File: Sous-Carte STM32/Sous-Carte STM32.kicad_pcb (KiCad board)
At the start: 2 copper layers, 113 x 120.1 mm, 34 parts, among them J1 RJ45, P1 CONN_25X2, P2 CONN_25X2, P3 CONN_4, P5 CONN_25X2, P6 CONN_2, P7 CONN_2, P8 CONN_2

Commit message: routage sous carte stm 32
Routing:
- net B7: track 0.00 -> 203.1 mm, vias 0 -> 2
- net B9: track 0.00 -> 173.4 mm, vias 0 -> 4
- net E5: track 0.00 -> 163.1 mm, vias 0 -> 2
- net C12: track 17.5 -> 175.9 mm, vias 0 -> 4
- net B5: track 0.00 -> 152.1 mm, vias 0 -> 2
- net B3: track 0.00 -> 144.2 mm, vias 0 -> 2
- net UART2_TX: track 39.9 -> 180.0 mm, vias 0 -> 2
- net C8: track 0.00 -> 107.3 mm, vias 0 -> 2
- net UART3_TX: track 37.6 -> 139.5 mm, vias 0 -> 2
- net UART4_TX: track 106.8 -> 114.2 mm
- net UART4_RX: track 129.0 -> 133.9 mm
- net D2: track 227.7 -> 230.7 mm
- net E8: track 0.00 -> 1.96 mm
- net E14: track 0.00 -> 1.96 mm
- net E12: track 0.00 -> 1.96 mm
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
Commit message: plus que 3 piste a router 2 ou trois truc a revoir
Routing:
- net E10: track 0.00 -> 167.1 mm, vias 0 -> 2
- net E8: track 1.96 -> 167.5 mm, vias 0 -> 2
- net E6: track 0.00 -> 157.5 mm, vias 0 -> 2
- net E4: track 0.00 -> 150.5 mm, vias 0 -> 2
- net E9: track 0.00 -> 124.6 mm, vias 0 -> 4
- net E12: track 1.96 -> 123.9 mm, vias 0 -> 2
- net C4: track 0.00 -> 118.9 mm, vias 0 -> 4
- net E14: track 1.96 -> 114.0 mm
- net A0: track 0.00 -> 108.5 mm, vias 0 -> 4
- net E7: track 0.00 -> 107.6 mm, vias 0 -> 2
- net E11: track 0.00 -> 107.0 mm, vias 0 -> 2
- net A2: track 0.00 -> 97.7 mm, vias 0 -> 4
- net B10: track 1.96 -> 98.6 mm, vias 0 -> 2
- net E13: track 0.00 -> 95.8 mm, vias 0 -> 4
- net E15: track 0.00 -> 89.3 mm, vias 0 -> 4
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
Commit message: routage sous carte stm32 fini reste a agrandir la carte
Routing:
- net B4: track 0.00 -> 182.9 mm, vias 0 -> 2
- net B6: track 0.00 -> 175.3 mm, vias 0 -> 2
- net B8: track 0.00 -> 168.2 mm, vias 0 -> 2
- net A0: track 108.5 -> 103.2 mm
- net B9: track 173.1 -> 178.3 mm
- net UART2_RX: track 183.3 -> 187.0 mm
- net E5: track 163.4 -> 162.7 mm
- net E6: track 157.5 -> 158.1 mm

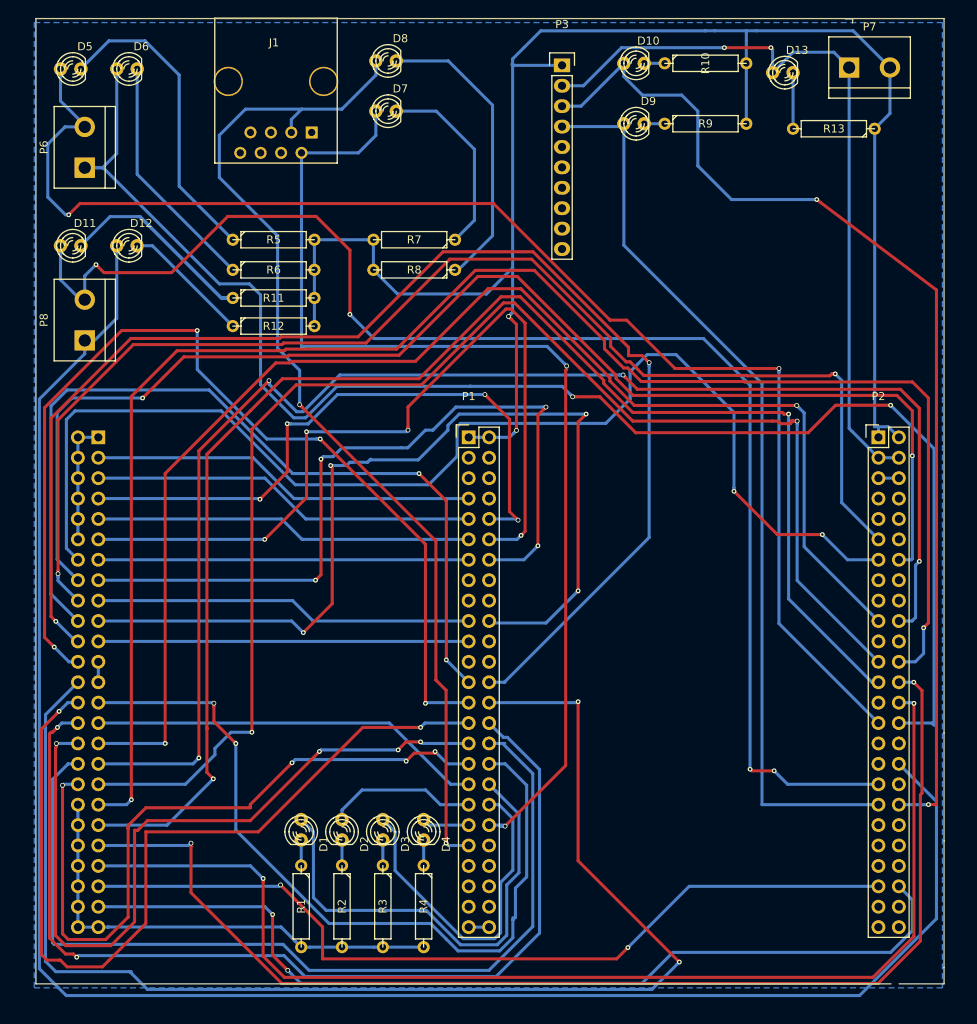
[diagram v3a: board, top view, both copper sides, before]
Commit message: agrandissement de la carte + ajout fil de masse
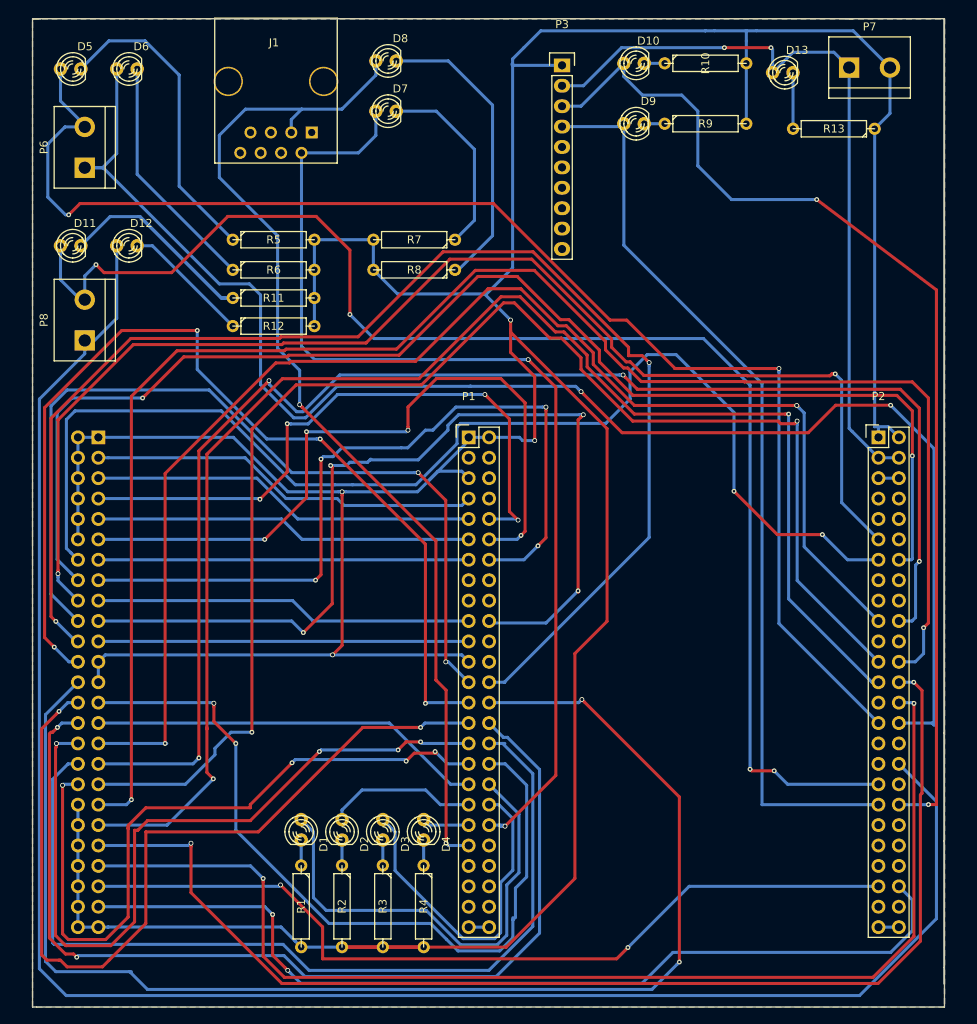
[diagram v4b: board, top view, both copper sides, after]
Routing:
- net GND: track 293.5 -> 541.7 mm, vias 2 -> 4
- net A0: track 103.2 -> 90.2 mm
- net UART3_TX: track 134.7 -> 131.3 mm
- net E4: track 150.5 -> 149.6 mm
- net C1: track 48.2 -> 48.9 mm
- net E10: track 167.1 -> 167.8 mm
- net E5: track 162.7 -> 163.3 mm
- net B8: track 168.2 -> 168.8 mm
- net B4: track 182.9 -> 183.5 mm
- net C4: track 118.9 -> 118.3 mm
- added copper zone on F.Cu, net GND
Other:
- board size 113 x 120.1 mm -> 113.5 x 123 mm

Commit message: début changement diamètre via
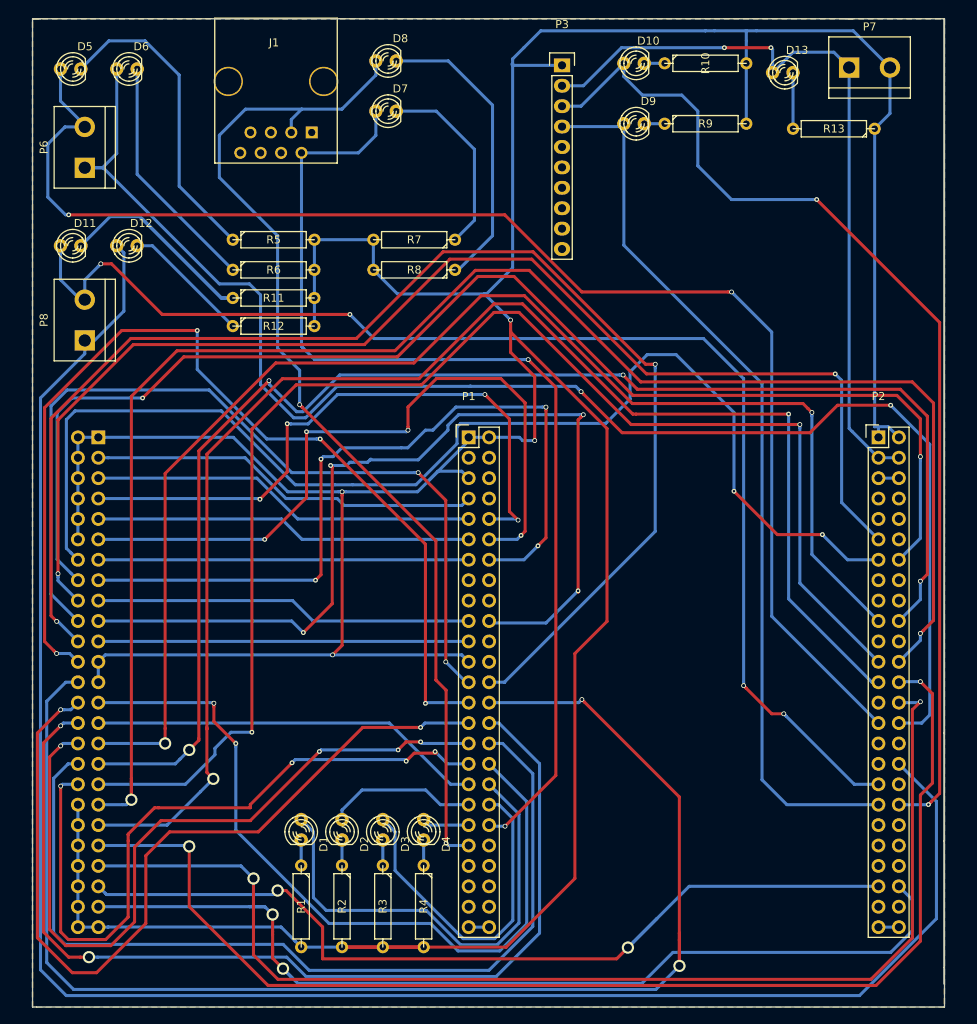
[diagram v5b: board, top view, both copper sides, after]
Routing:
- net C12: track 175.9 -> 159.6 mm
- net C8: track 107.0 -> 112.4 mm
- net C9: track 117.2 -> 121.9 mm
- net E10: track 167.8 -> 172.2 mm
- net B5: track 150.1 -> 152.5 mm
- net B6: track 175.7 -> 173.6 mm
- net UART4_TX: track 114.2 -> 112.4 mm
- net B8: track 168.8 -> 167.0 mm
- net UART2_RX: track 187.0 -> 185.3 mm
- net E11: track 107.0 -> 105.4 mm
- net B4: track 183.5 -> 181.9 mm
- net UART4_RX: track 133.9 -> 132.4 mm
- net B3: track 145.9 -> 147.4 mm
- net B10: track 98.7 -> 97.2 mm
- net B9: track 178.3 -> 176.9 mm
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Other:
- net class Default: via_dia 0.6 -> 1.524; via_drill 0.4 -> 1

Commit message: remplacement via
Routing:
- net E10: track 172.2 -> 186.7 mm
- net UART4_RX: track 132.4 -> 139.8 mm
- net B10: track 97.2 -> 104.0 mm
- net E4: track 149.6 -> 156.0 mm
- net E6: track 157.3 -> 163.6 mm
- net E9: track 124.9 -> 131.1 mm
- net E8: track 168.1 -> 173.2 mm
- net E5: track 162.4 -> 167.2 mm
- net GND: track 541.7 -> 546.5 mm
- net 5V: track 95.1 -> 99.3 mm
- net D2: track 232.3 -> 235.9 mm
- net B3: track 147.4 -> 150.4 mm
- net C12: track 159.6 -> 162.4 mm
- net B9: track 176.9 -> 179.6 mm
- net B6: track 173.6 -> 176.1 mm
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- removed copper zone on B.Cu, net GND
- removed copper zone on F.Cu, net GND
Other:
- board size 113.5 x 123 mm -> 117.5 x 123 mm

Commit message: remplacement presque terminé
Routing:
- net GND: track 546.5 -> 580.0 mm
- net E13: track 96.2 -> 103.5 mm
- net E9: track 131.1 -> 137.7 mm
- net E5: track 167.2 -> 173.7 mm
- net C4: track 116.9 -> 112.3 mm
- net B9: track 179.6 -> 183.4 mm
- net D9: track 130.5 -> 134.1 mm
- net A0: track 89.6 -> 92.1 mm
- net E7: track 109.2 -> 111.7 mm
- net E11: track 106.1 -> 108.3 mm
- net A2: track 97.4 -> 95.3 mm
- net C2: track 78.3 -> 80.1 mm
- net B8: track 167.0 -> 168.2 mm
- net C1: track 48.9 -> 49.5 mm

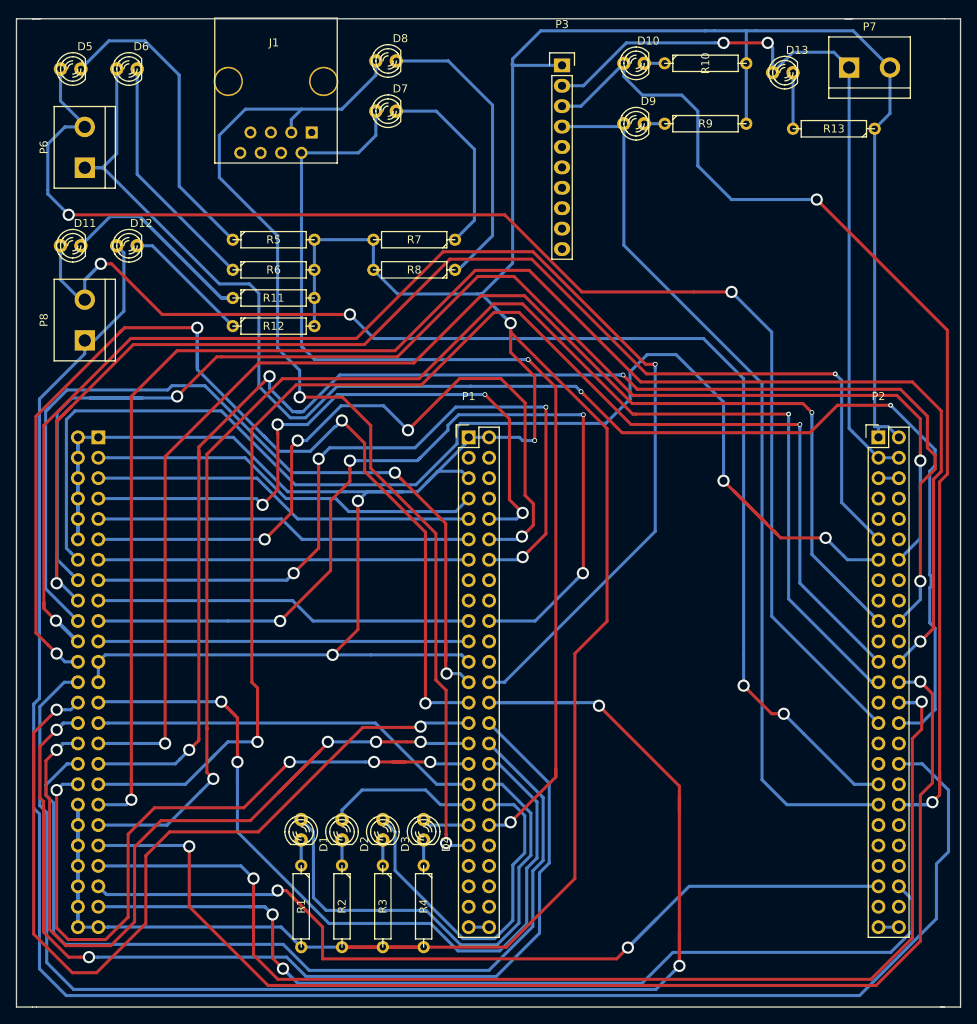
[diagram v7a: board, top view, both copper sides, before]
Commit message: via totalement remplacés (à verifier) + DRC ok
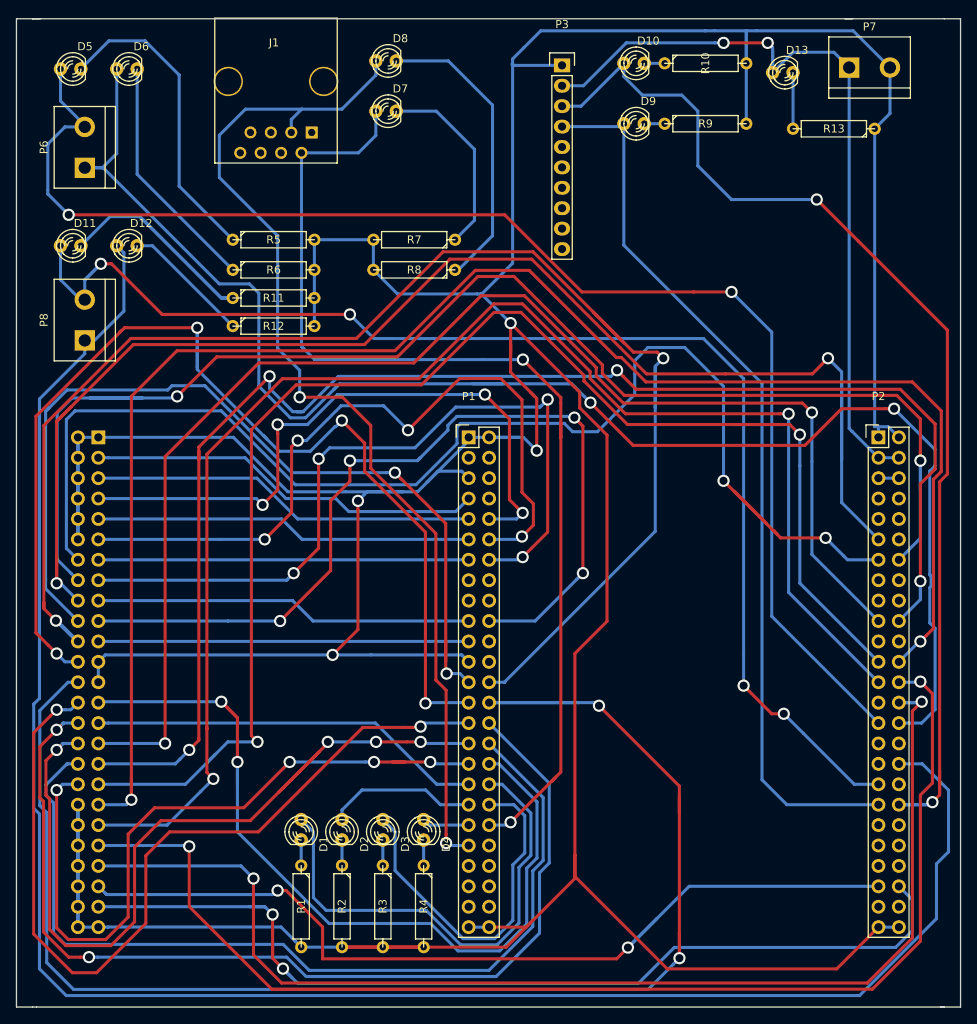
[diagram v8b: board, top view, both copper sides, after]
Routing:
- net GND: track 580.0 -> 642.6 mm
- net E8: track 173.2 -> 185.5 mm
- net E6: track 163.6 -> 175.7 mm
- net B6: track 176.1 -> 182.3 mm
- net UART2_RX: track 186.8 -> 192.8 mm
- net E4: track 156.0 -> 159.2 mm
- net UART3_TX: track 131.6 -> 133.8 mm
- net A2: track 95.3 -> 97.0 mm
- net C4: track 112.3 -> 111.2 mm
- net E10: track 186.7 -> 185.8 mm
- net E5: track 173.7 -> 174.4 mm
- net B8: track 168.2 -> 168.8 mm
